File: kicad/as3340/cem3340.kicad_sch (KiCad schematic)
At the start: 64 parts, among them U10 LM79L05, U11 LM393, U2 TL074, U3 AS3340, U8 DG442CY+, U9 DG442CY+

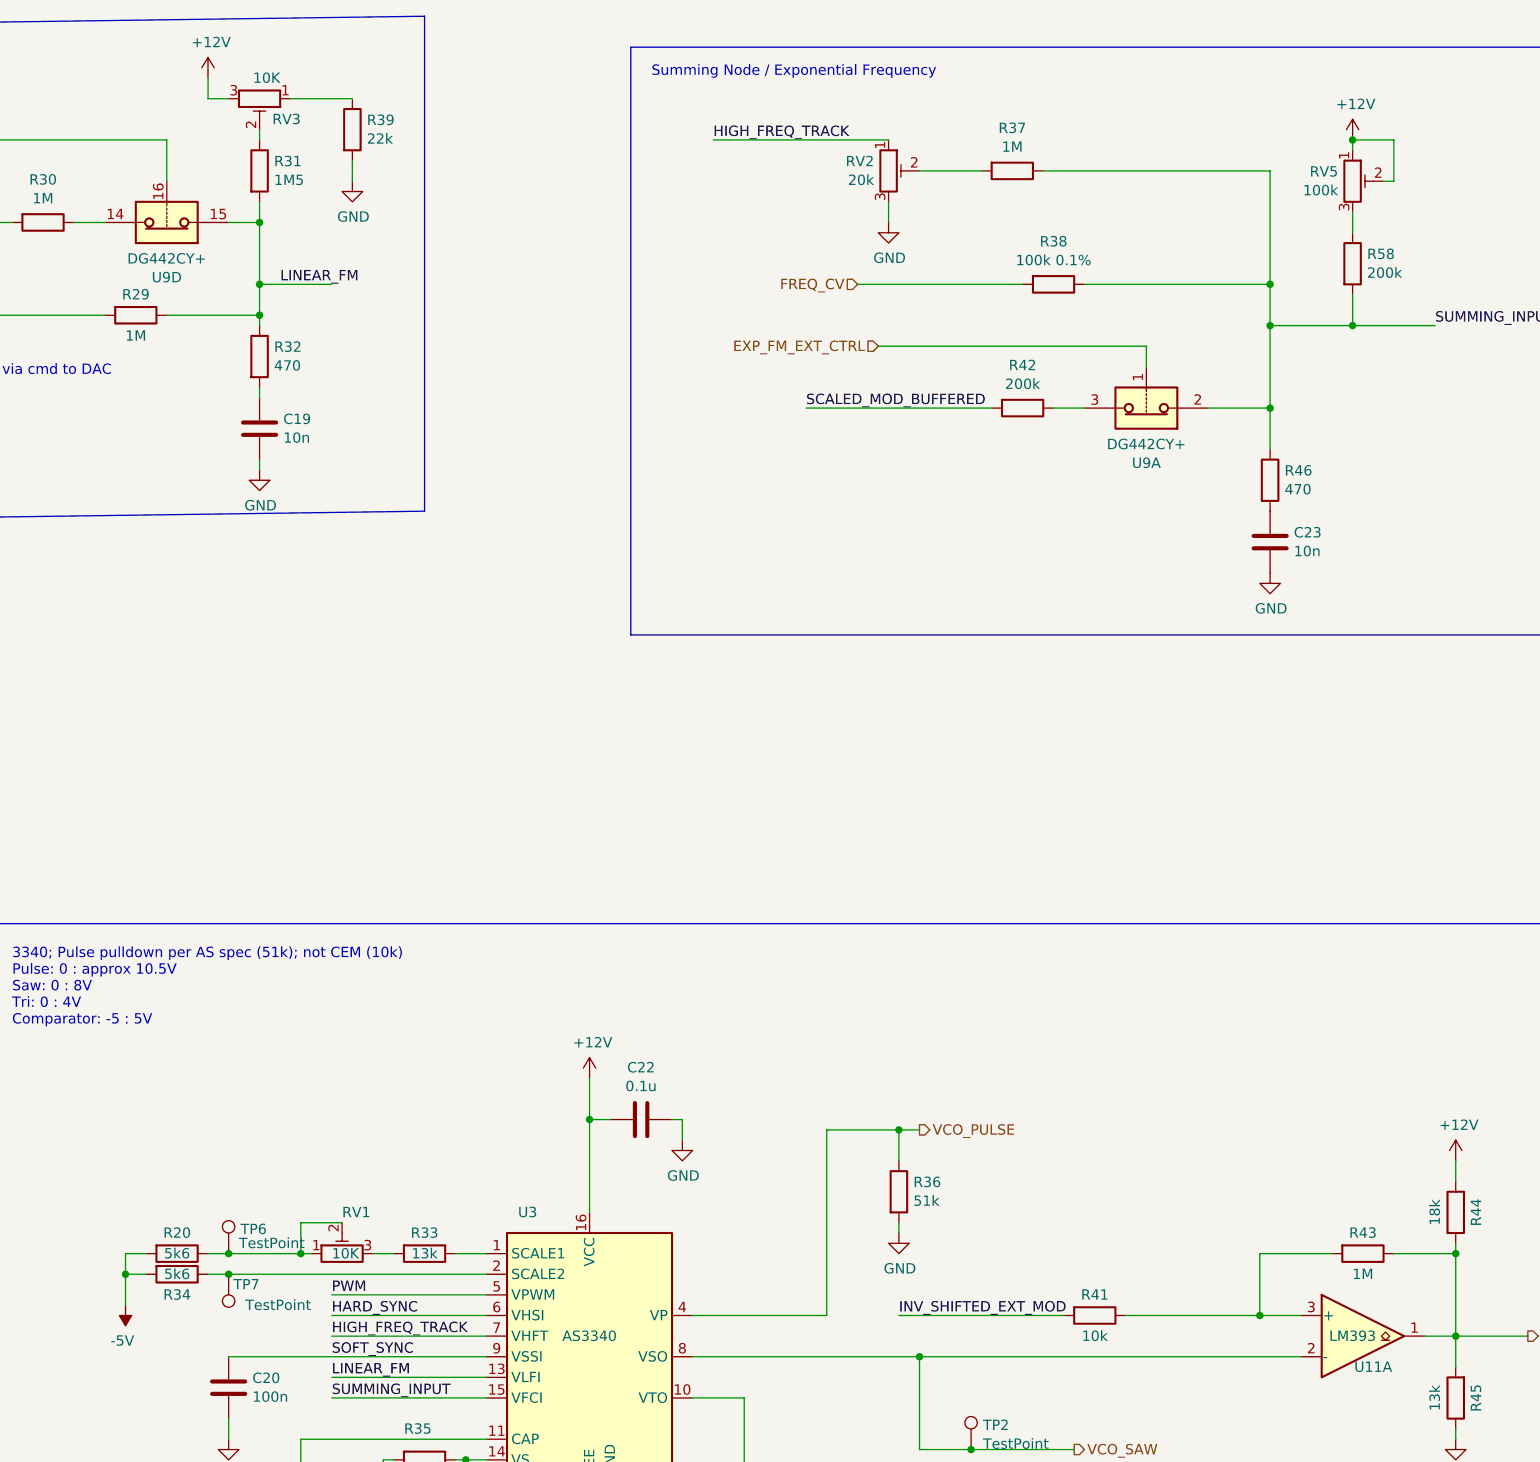
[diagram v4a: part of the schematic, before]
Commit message: going back to two trimmer method
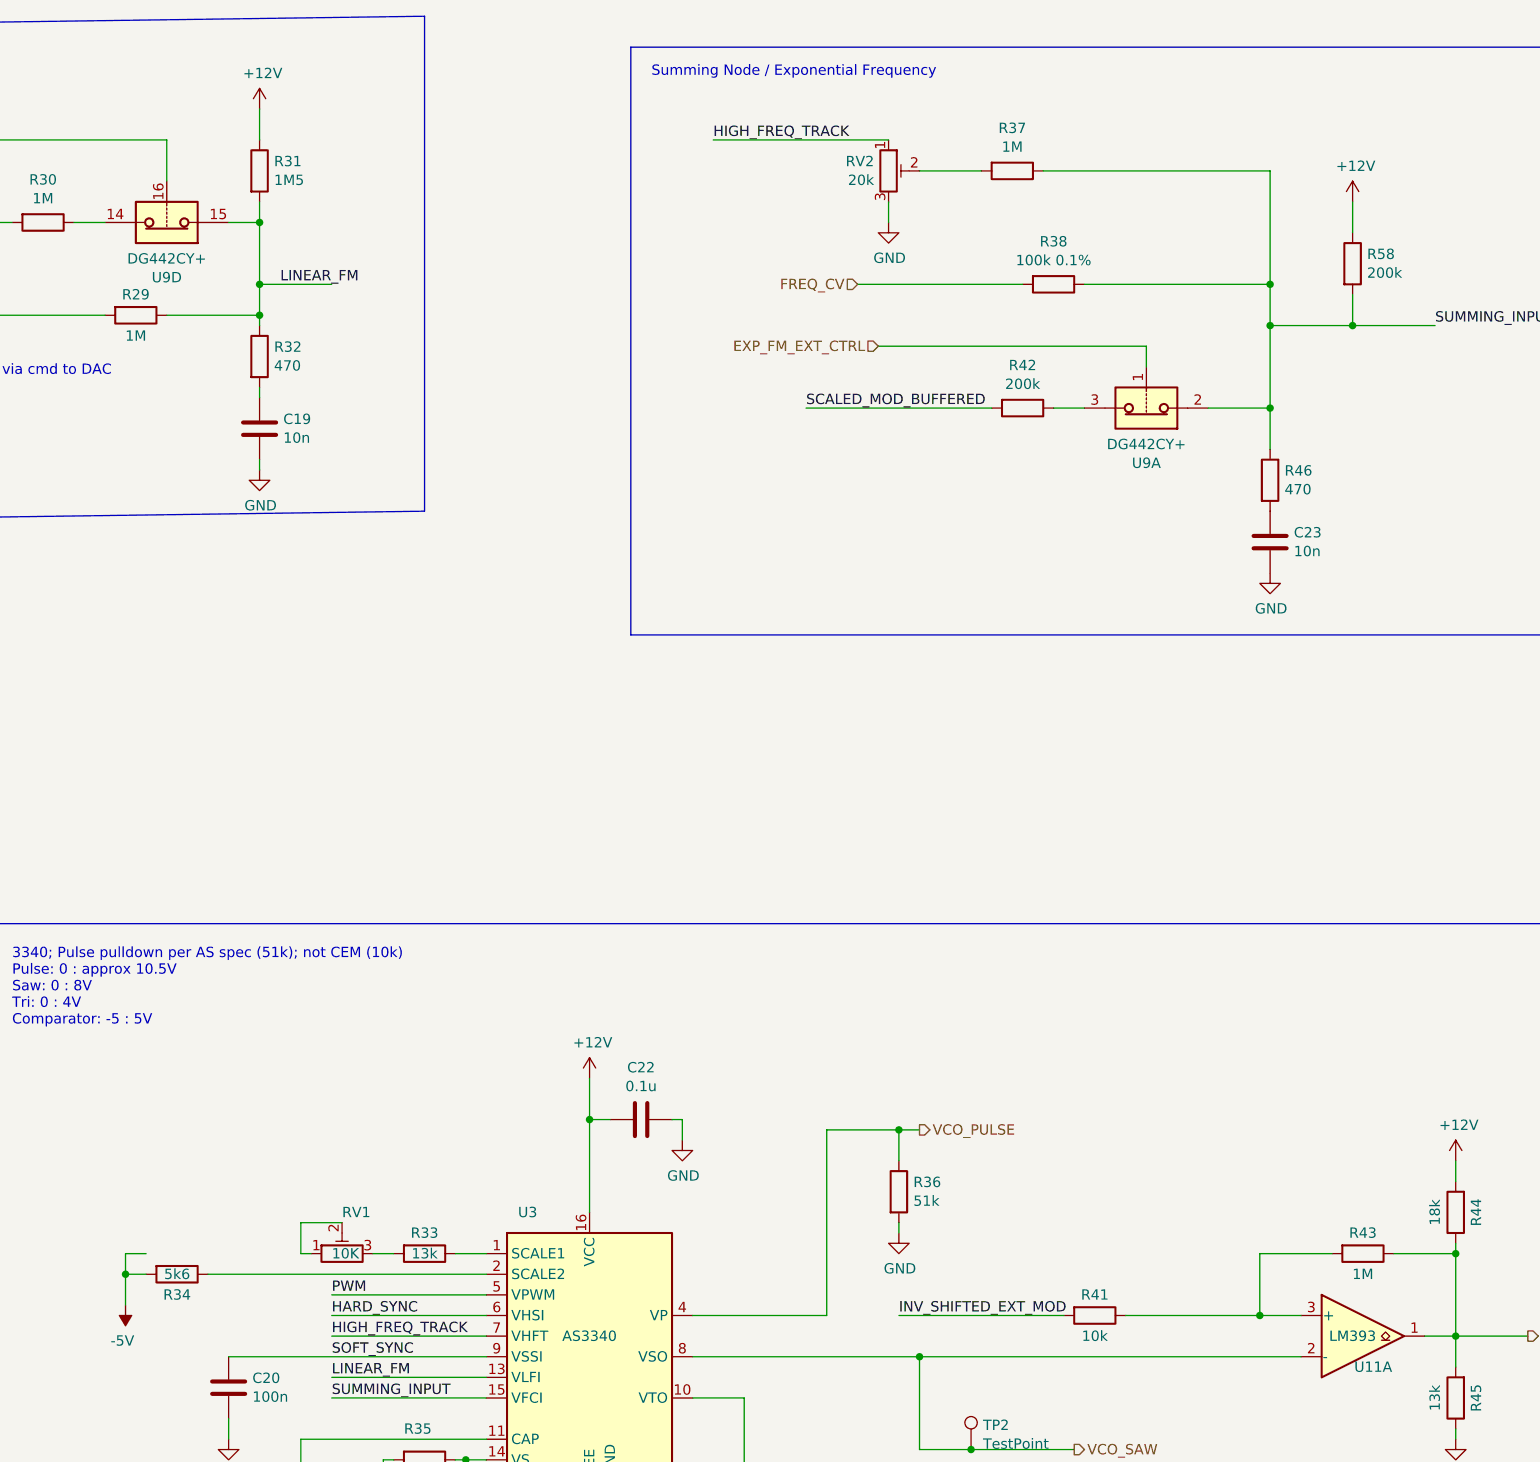
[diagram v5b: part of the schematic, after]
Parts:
- removed R20: 5k6, Resistor_SMD:R_0603_1608Metric, symbol Device:R
- removed R39: 22k, Resistor_SMD:R_0603_1608Metric, symbol Device:R
- removed RV3: 10K, Potentiometer_THT:Potentiometer_Bourns_3296W_Vertical, symbol as3340:R_POT_TRIM-Device
- removed RV5: 100k, Potentiometer_THT:Potentiometer_Bourns_3296W_Vertical, symbol as3340:R_POT_TRIM-Device
- removed TP6, TP7: TestPoint, TestPoint:TestPoint_Pad_2.0x2.0mm, symbol Connector:TestPoint
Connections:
- net +12V: now also R31.1, R58.1

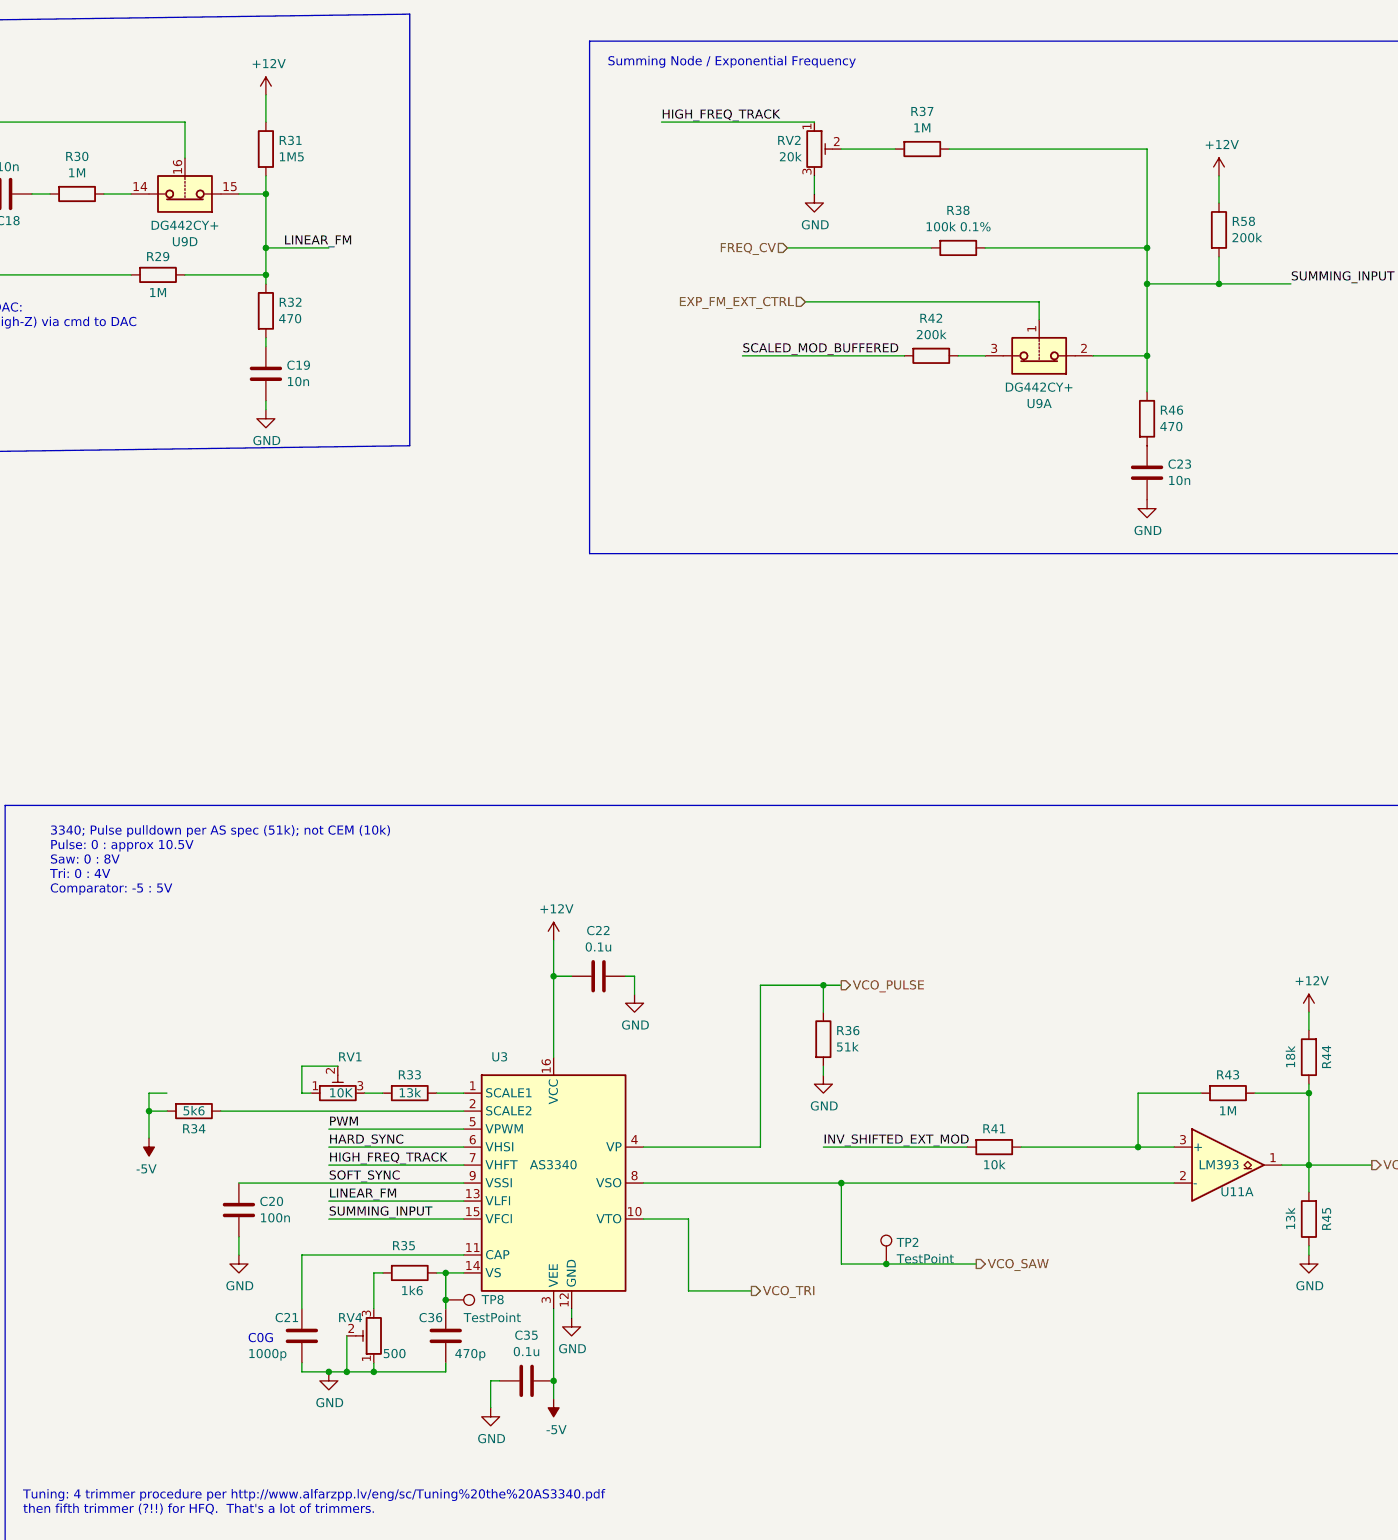
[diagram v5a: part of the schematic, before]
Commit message: pcb cleanup, get volt ref in
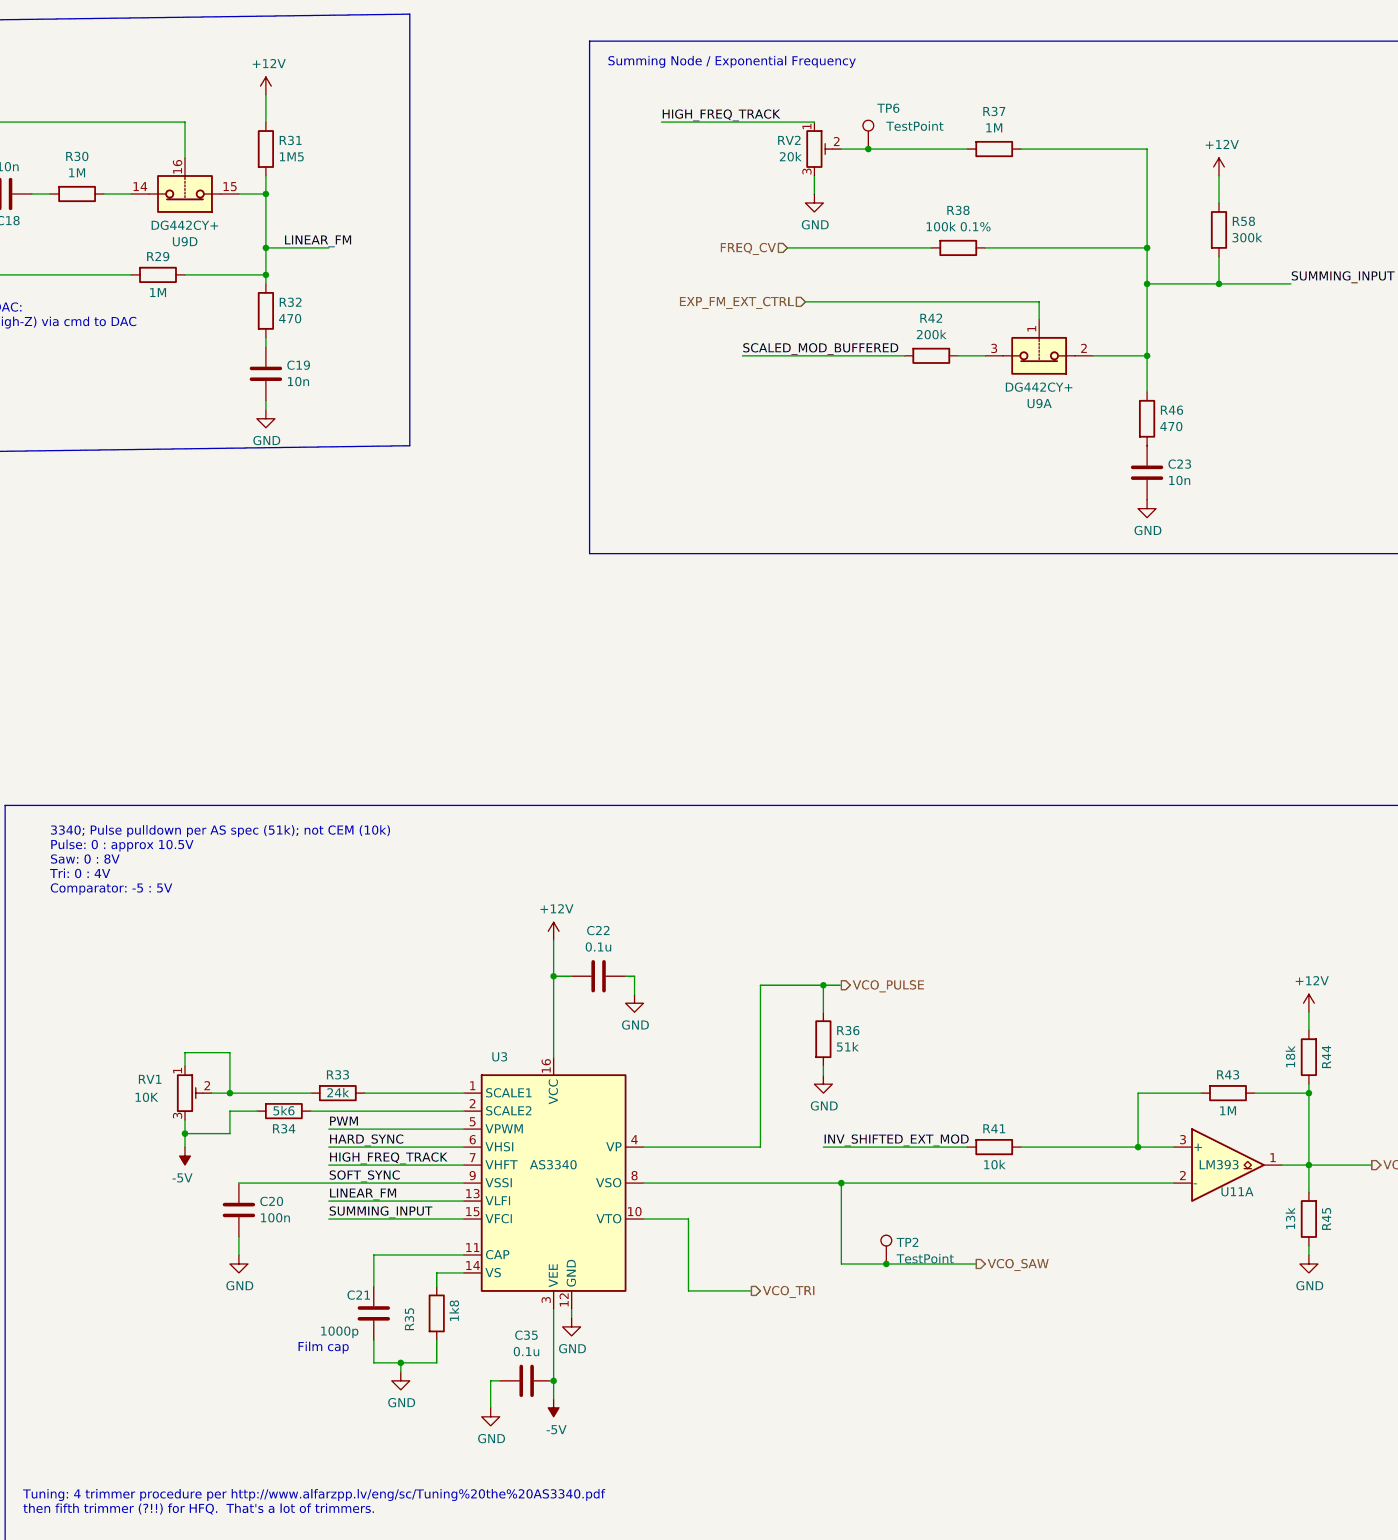
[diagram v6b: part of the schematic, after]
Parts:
- removed C36: 470p, Capacitor_SMD:C_0603_1608Metric, symbol Device:C
- removed RV4: 500, Potentiometer_THT:Potentiometer_Bourns_3296W_Vertical, symbol as3340:R_POT_TRIM-Device
- removed TP8: TestPoint, TestPoint:TestPoint_Pad_2.0x2.0mm, symbol Connector:TestPoint
- added TP6: TestPoint, TestPoint:TestPoint_Pad_2.0x2.0mm, symbol Connector:TestPoint
- R33: value 13k -> 24k; LCSC Part C22797 -> C23352
- R35: value 1k6 -> 1k8; LCSC Part C22847 -> C4177
- R58: value 200k -> 300k; LCSC Part (none) -> C23024
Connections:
- net -5V: now also RV1.3
- net GND: now also R35.2
- net at R33.2: now also RV1.1, RV1.2; no longer RV1.3
- net at R37.2, RV2.2: now also TP6.1
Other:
- note added: "Film cap"
- note removed: "C0G"
- moved on the sheet: C21, R33, R34, R35, R37, RV1

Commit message: fixes for BOM
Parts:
- C18, C19, C23: LCSC C57112 -> (none)
- C20, C22, C35: LCSC C14663 -> (none)
- RV1: LCSC C118954 -> (none)
- RV2: LCSC C118936 -> (none)
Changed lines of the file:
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@@
       (effects (font (size 1.27 1.27)) hide)
     )
-    (property "LCSC" "C118954" (id 4) (at 228.6 165.1 0)
+    (property "LCSC" "" (id 4) (at 228.6 165.1 0)
       (effects (font (size 1.27 1.27)) hide)
     )
@@
       (effects (font (size 1.27 1.27)) hide)
     )
-    (property "LCSC" "C118936" (id 4) (at 317.5 31.75 0)
+    (property "LCSC" "" (id 4) (at 317.5 31.75 0)
       (effects (font (size 1.27 1.27)) hide)
     )
@@
       (effects (font (size 1.27 1.27)) hide)
     )
-    (property "LCSC" "C57112" (id 4) (at 364.49 77.47 0)
+    (property "LCSC" "" (id 4) (at 364.49 77.47 0)
       (effects (font (size 1.27 1.27)) hide)
     )
@@
       (effects (font (size 1.27 1.27)) hide)
     )
-    (property "LCSC" "C14663" (id 4) (at 236.22 181.61 0)
+    (property "LCSC" "" (id 4) (at 236.22 181.61 0)
       (effects (font (size 1.27 1.27)) hide)
     )
@@
       (effects (font (size 1.27 1.27)) hide)
     )
-    (property "LCSC" "C57112" (id 4) (at 240.03 63.5 0)
+    (property "LCSC" "" (id 4) (at 240.03 63.5 0)
       (effects (font (size 1.27 1.27)) hide)
     )
@@
       (effects (font (size 1.27 1.27)) hide)
     )
-    (property "LCSC" "C14663" (id 4) (at 287.02 148.59 90)
+    (property "LCSC" "" (id 4) (at 287.02 148.59 90)
       (effects (font (size 1.27 1.27)) hide)
     )
@@
       (effects (font (size 1.27 1.27)) hide)
     )
-    (property "LCSC" "C57112" (id 4) (at 203.2 38.1 0)
+    (property "LCSC" "" (id 4) (at 203.2 38.1 0)
       (effects (font (size 1.27 1.27)) hide)
     )
@@
       (effects (font (size 1.27 1.27)) hide)
     )
-    (property "LCSC" "C14663" (id 4) (at 276.86 205.74 90)
-      (effects (font (size 1.27 1.27)) hide)
-    )
+    (property "LCSC" "" (id 4) (at 276.86 205.74 90)
+      (effects (font (size 1.27 1.27)) hide)
+    )

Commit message: update title block and add schematic pdf
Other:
- title: Zoxnoxious 3340 Oscillator: 3340 Primary -> Zoxnoxious 3340 Oscillator
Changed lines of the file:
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@@
   (paper "B")
   (title_block
-    (title "Zoxnoxious 3340 Oscillator: 3340 Primary")
-    (rev "0.3")
+    (title "Zoxnoxious 3340 Oscillator")
+    (rev "0.4")
     (company "Zoxnoxious Engineering")
   )
